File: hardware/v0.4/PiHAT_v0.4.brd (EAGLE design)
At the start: 65 x 56.5 mm, 40 parts, among them IC1 BMP280, J1 FTDI, J3 ISP, U1 ATMEGA328P, U10 TSL2591, U3 OPA344, U6 ADMP401, U8 CCS811, Y1 16MHZ

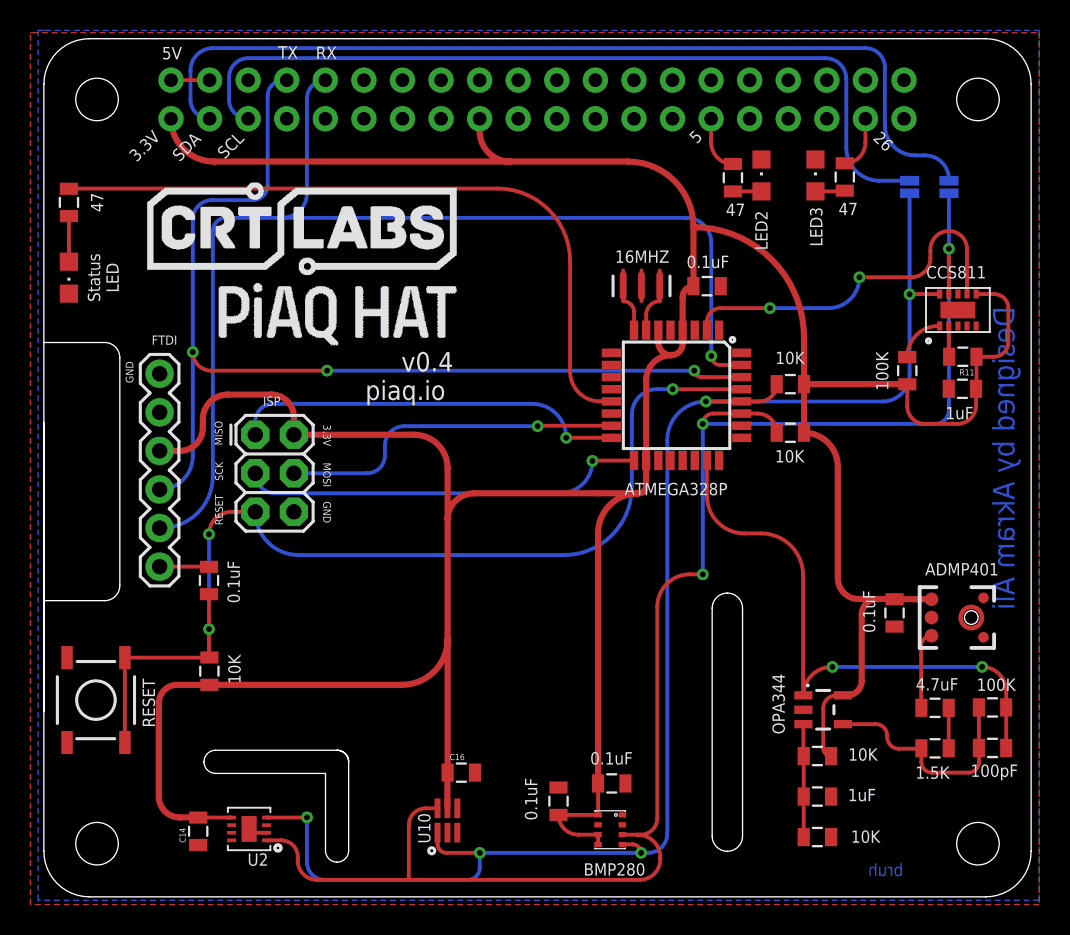
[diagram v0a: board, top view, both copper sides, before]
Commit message: v0.4 - update
Relocated SHT31/35 sensor location to be on a 'cooler' spot over the Pi
Added extra rullup resistor on CCS811 to make it stable during startups
trace adjustments
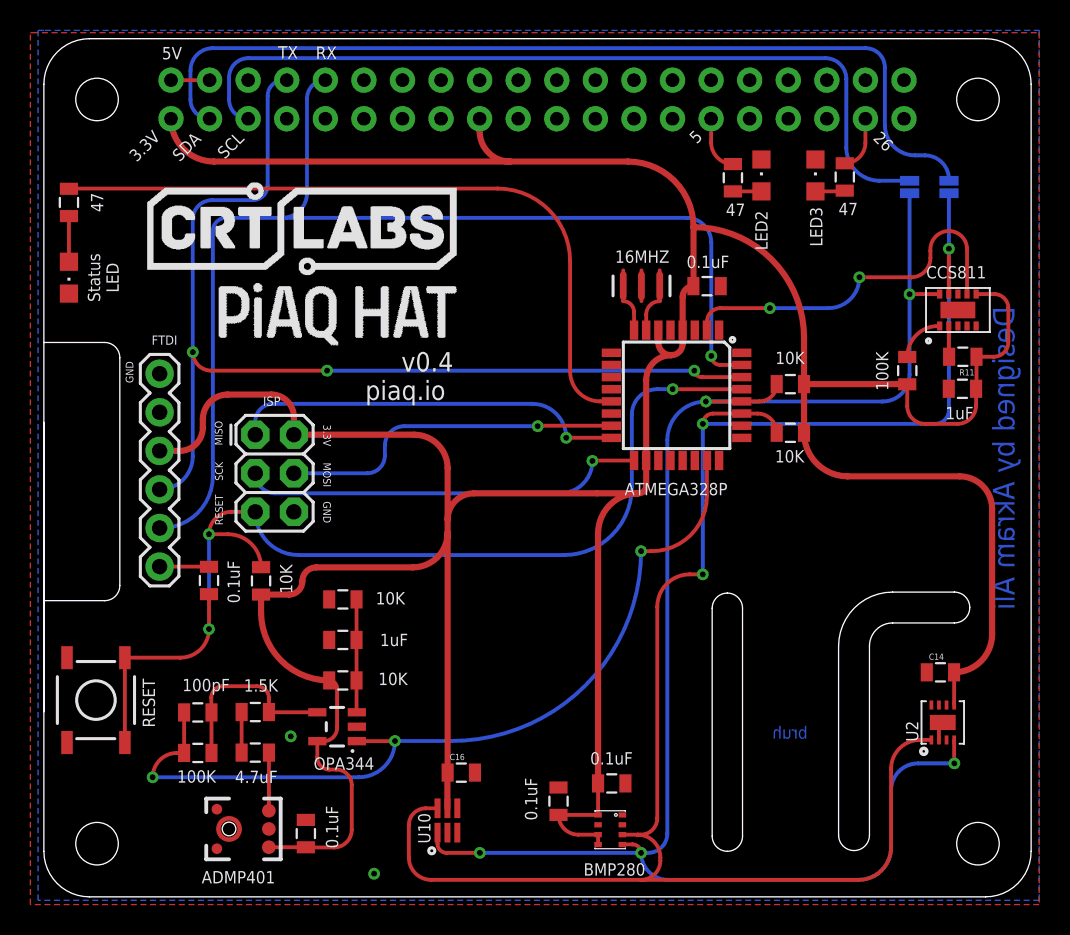
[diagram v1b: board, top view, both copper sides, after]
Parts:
- moved R8 52.4 mm to (10.1, 8.20), turned to 0 degrees
- moved C2 52.4 mm to (10.1, 10.9), turned to 180 degrees
- moved U6 50.8 mm to (12.2, 3.20), turned to 270 degrees
- moved C14 50.0 mm to (59.0, 13.5), turned to 0 degrees
- moved U2 46.2 mm to (59.2, 10.2), turned to 90 degrees
- moved C8 44.9 mm to (13.9, 8.23), turned to 180 degrees
- moved R3 44.8 mm to (13.9, 10.9), turned to 180 degrees
- moved C10 41.4 mm to (17.2, 2.90), turned to 90 degrees
- moved R1 34.9 mm to (19.7, 18.3), turned to 0 degrees
- moved C9 32.9 mm to (19.7, 15.6), turned to 180 degrees
- moved U3 32.0 mm to (19.3, 9.93), turned to 90 degrees
- moved R7 31.6 mm to (19.7, 13.0), turned to 180 degrees
- moved R13 6.85 mm to (14.3, 19.5)
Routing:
- net A0: track 37.3 -> 54.4 mm, vias 2 -> 3
- net SDA: track 105.9 -> 120.5 mm
- net SCL: track 99.6 -> 109.1 mm
- net VCC: track 252.7 -> 258.6 mm
- net RESET: track 65.8 -> 69.0 mm
- net N$10: track 14.8 -> 12.2 mm
- net N$7: track 5.04 -> 3.83 mm
- net GND: vias 0 -> 2

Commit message: Adjusted silkscreen
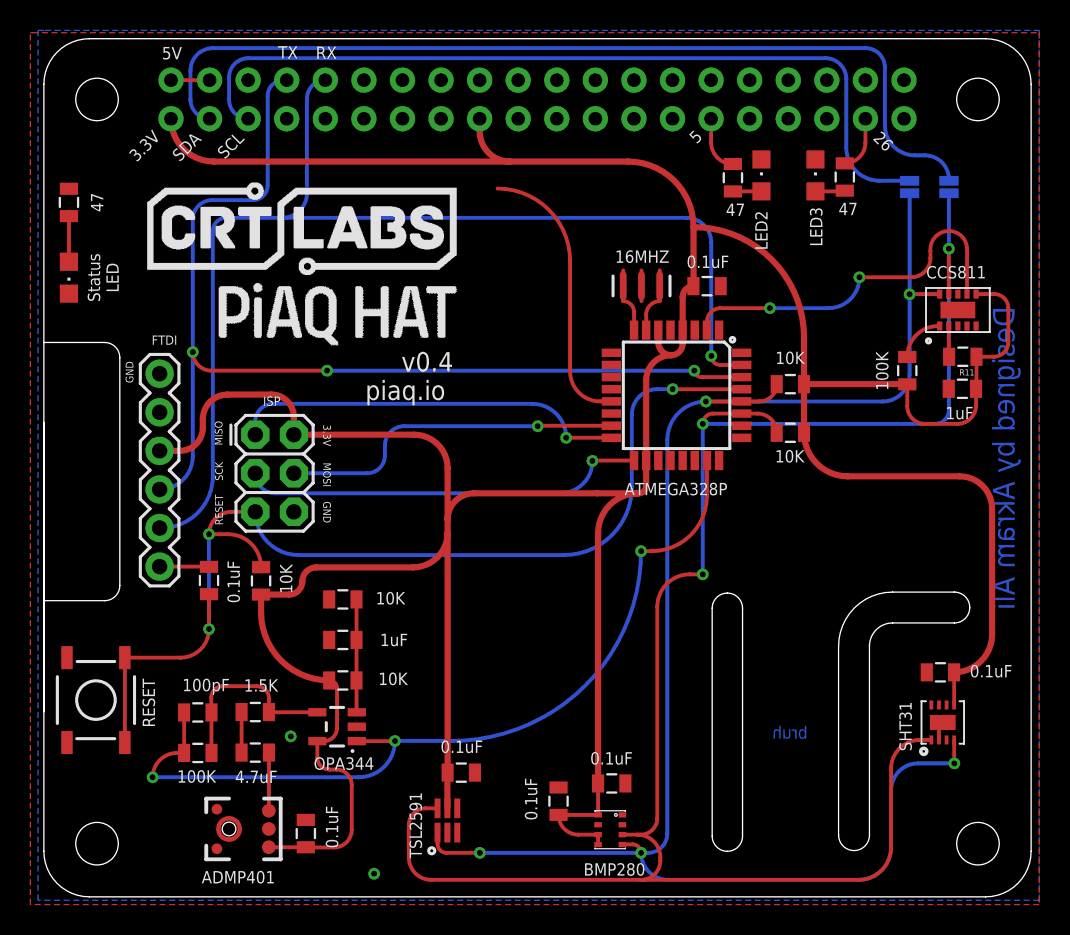
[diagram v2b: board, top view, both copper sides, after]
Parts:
- U2: value (none) -> SHT31
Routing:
- net N$2: track 45.8 -> 17.6 mm

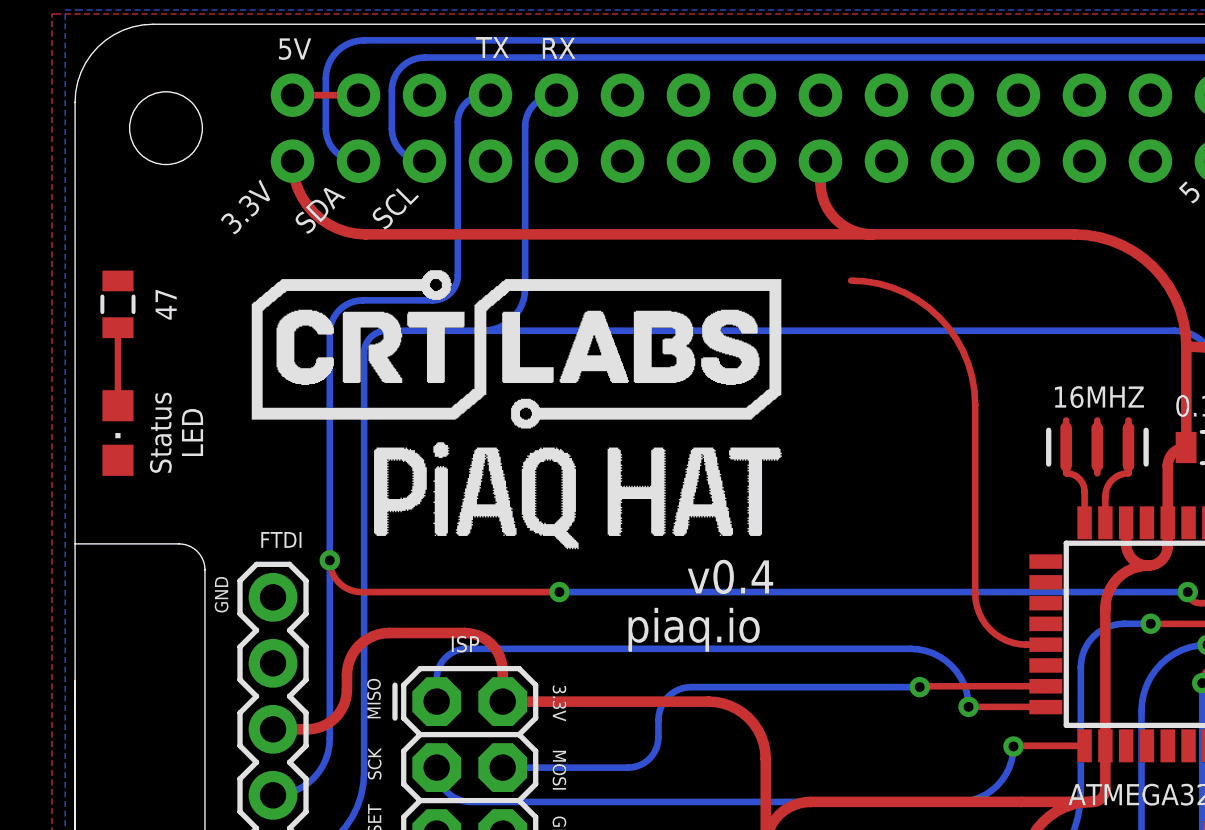
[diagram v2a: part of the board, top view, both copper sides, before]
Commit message: Added RGB LED
- RGB LED on pin 6
- Rearragned other LED on pin 9 and adjusted trace
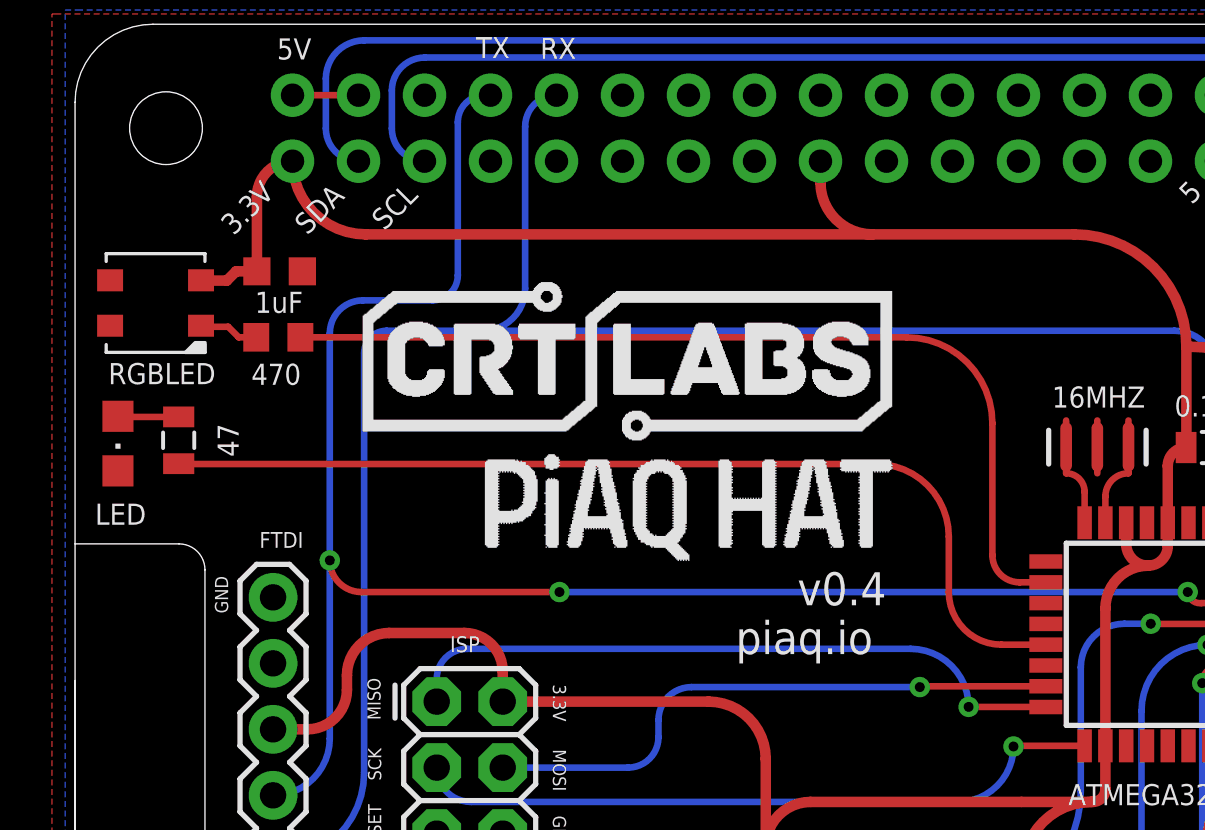
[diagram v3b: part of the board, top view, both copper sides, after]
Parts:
- added C3: 1uF, adafruit:C0603K
- added R16: 470, adafruit:R0603
- added RGBLED: WS2812B3535, adafruit:LED3535
- moved R4 5.73 mm to (3.99, 39.2), turned to 90 degrees
- moved LED1 0.41 mm to (1.65, 39.1)
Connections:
- new net D6: R16.2, U1.10
- new net N$12: R16.1, RGBLED.1
- net GND: now also C3.2, RGBLED.4
- net VCC: now also C3.1, RGBLED.2
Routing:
- net D6: track 0.00 -> 35.6 mm
- net N$2: track 17.6 -> 37.5 mm
- net VCC: track 258.6 -> 265.7 mm
- net N$12: track 0.00 -> 2.31 mm
- net N$3: track 3.00 -> 2.35 mm
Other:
- board text added: "LED"
- board text removed: "Status LED"
